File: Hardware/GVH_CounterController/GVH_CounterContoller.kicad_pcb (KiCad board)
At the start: 2 copper layers, 82.5 x 88.9 mm, 74 parts, among them J1 Molex Ultra-Fit, J10 Molex Micro-Fit 2pos, J11 Molex Micro-Fit 2pos, J12 Molex Micro-Fit 2pos, J13 Molex Micro-Fit 3pos, J2 Molex Micro-Fit 2pos, J3 WIZnet_J1B1211CCD_RJ45, J4 Molex Micro-Fit 5pos, J5 Molex Micro-Fit 5pos, J6 Molex Micro-Fit 5pos, J7 Molex Micro-Fit 5pos, J8 Molex Micro-Fit 2pos, J9 Molex Micro-Fit 2pos, K1 Relay_DPDT, Q1 MBT2222, Q2 AO3406, Q3 AO3406, SW1 SW_DIP_x02, SW2 SW_MEC_5G, U1 Teensy4.1, U10 74LVC2G125DC,125, U11 74LVC2G125DC,125, U12 74LVC2G125DC,125, U14 SN74LVC2G17, U2 R-78E5.0-1.0, U3 RT9080-3.3, U4 DS18B20_, U5 74LVC2G125DC,125, U6 74LVC2G125DC,125, U7 74LVC2G125DC,125, U8 74LVC2G125DC,125, U9 74LVC2G125DC,125

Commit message: Checkpoint before rerouting the power supply
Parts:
- moved J13 89.5 mm to (90.4, 102.8)
- moved R7 7.39 mm to (151.4, 64.0), turned to -90 degrees
- moved C3 1.30 mm to (139.7, 114.3)
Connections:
- SW2 pad 2: BUTTON -> GND
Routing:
- net +12V: track 35.6 -> 125.1 mm
- net +3.3V: track 94.7 -> 171.7 mm, vias 2 -> 1
- net +5V: track 78.7 -> 130.2 mm

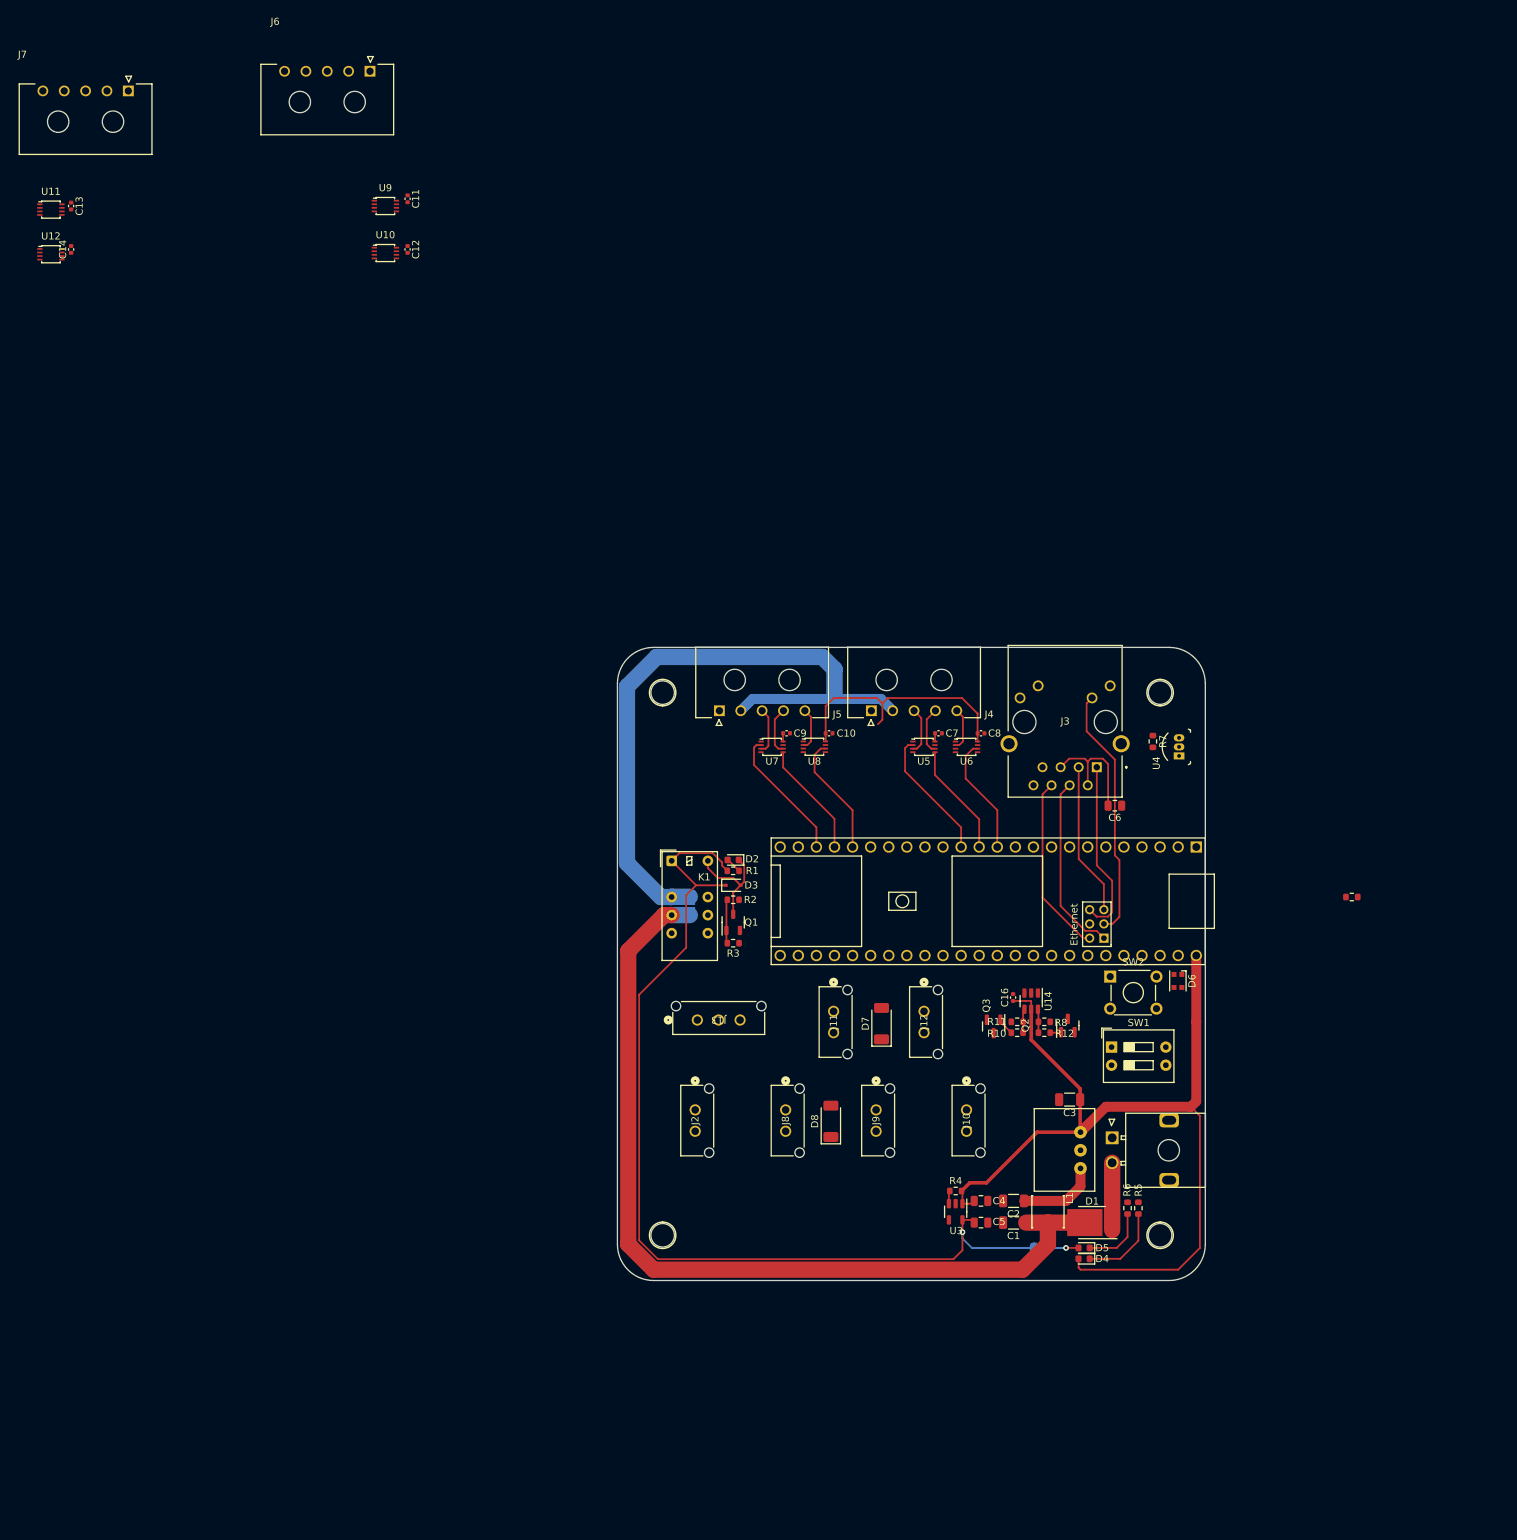
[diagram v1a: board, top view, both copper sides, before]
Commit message: Added header for two board stack design
This will allow the fans to be connected horizontally
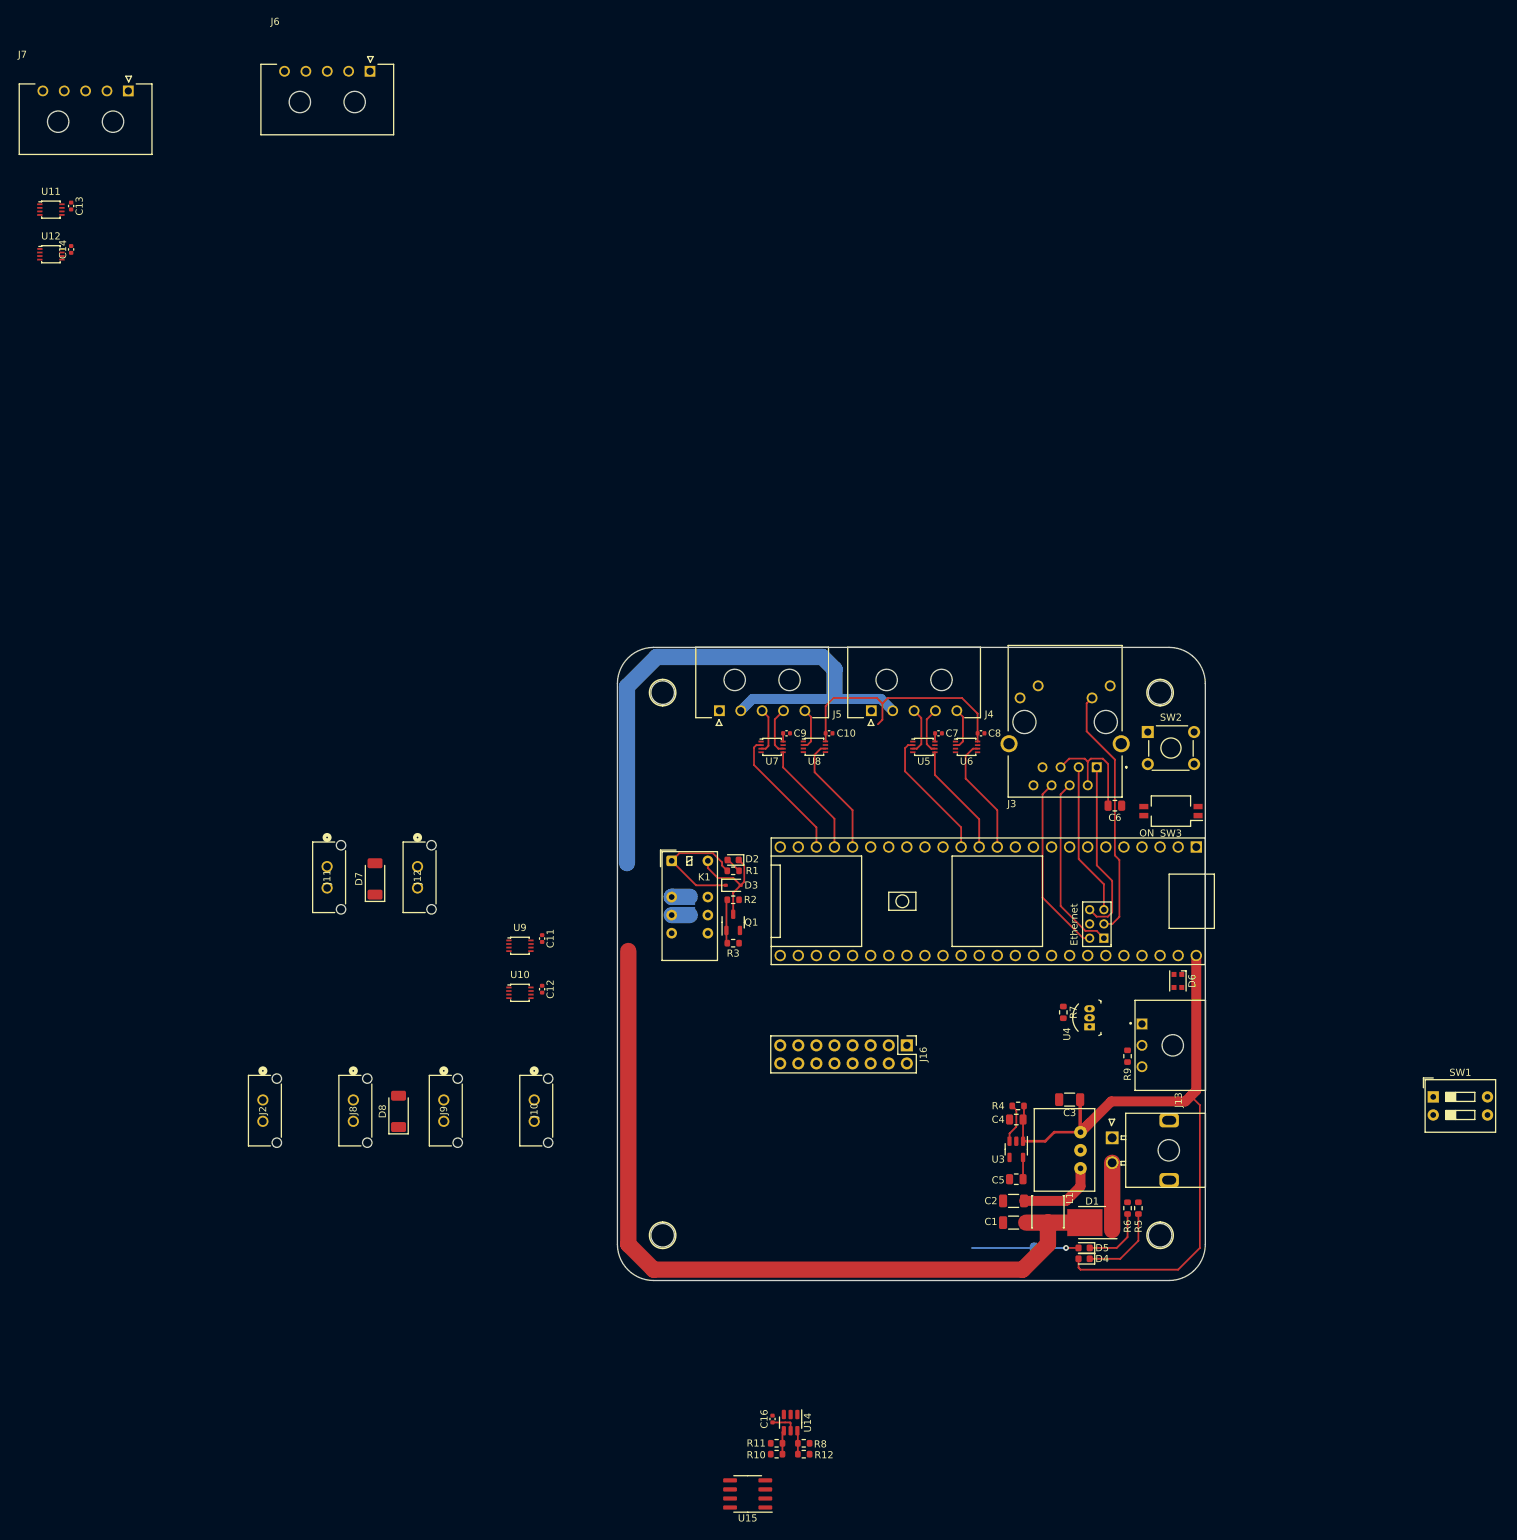
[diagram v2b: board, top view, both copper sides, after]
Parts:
- removed Q2, Q3: AO3406, Package_TO_SOT_SMD:SOT-23
- added J16: Conn_02x08_Odd_Even, Connector_PinHeader_2.54mm:PinHeader_2x08_P2.54mm_Vertical, F.Cu at (116.8, 106.7)
- added SW3: SW_DIP_x02, Button_Switch_SMD:SW_DIP_SPSTx02_Slide_KingTek_DSHP02TS_W7.62mm_P1.27mm, F.Cu at (153.9, 73.8)
- added U15: AO4882, Package_SO:SOIC-8_3.9x4.9mm_P1.27mm, F.Cu at (94.5, 169.7)
- J13: footprint 0_connector:MOLEX_MICROFIT-VERT-3POS_436500315 -> 0_connector:MOLEX_MICROFIT-RA-3POS_436500300
- moved U10 105.6 mm to (62.5, 99.3)
- moved C11 105.6 mm to (65.6, 91.7)
- moved C12 105.6 mm to (65.6, 98.8)
- moved U9 105.6 mm to (62.5, 92.7)
- moved D7 74.0 mm to (42.2, 83.3)
- moved J11 74.0 mm to (35.7, 83.1)
- moved J12 74.0 mm to (48.4, 83.1)
- moved C16 68.1 mm to (98.0, 159.1)
- moved R12 68.1 mm to (102.4, 162.6)
- moved R8 68.1 mm to (102.4, 164.1)
- moved R10 68.1 mm to (98.6, 164.1)
- moved R11 68.1 mm to (98.6, 162.6)
- moved U14 68.1 mm to (100.5, 159.7)
- moved J10 60.7 mm to (64.8, 115.8)
- moved J2 60.7 mm to (26.7, 115.8)
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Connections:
- net Net-(J4-Pin_3) renamed /IO_Level_Shift/CLK_OUT
- net Net-(J4-Pin_4) renamed /IO_Level_Shift/LOAD_OUT
- net Net-(J4-Pin_5) renamed /IO_Level_Shift/SERIAL_IN
- net Net-(J5-Pin_3) renamed /IO_Level_Shift1/CLK_OUT
- net Net-(J5-Pin_4) renamed /IO_Level_Shift1/LOAD_OUT
- net Net-(J5-Pin_5) renamed /IO_Level_Shift1/SERIAL_IN
- U10 pad 2: Net-(J6-Pin_5) -> /IO_Level_Shift2/SERIAL_IN
- U10 pad 6: /IO_Level_Shift2/SERIAL_IN -> (no net)
- U11 pad 2: /IO_Level_Shift3/LOAD -> (no net)
- U11 pad 3: Net-(J7-Pin_3) -> (no net)
- U11 pad 5: /IO_Level_Shift3/CLK -> (no net)
- U11 pad 6: Net-(J7-Pin_4) -> (no net)
- U12 pad 2: Net-(J7-Pin_5) -> /IO_Level_Shift3/SERIAL_IN
- U12 pad 6: /IO_Level_Shift3/SERIAL_IN -> (no net)
- U9 pad 2: /IO_Level_Shift2/LOAD -> (no net)
- U9 pad 3: Net-(J6-Pin_3) -> (no net)
- U9 pad 5: /IO_Level_Shift2/CLK -> (no net)
- U9 pad 6: Net-(J6-Pin_4) -> (no net)
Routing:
- net +3.3V: track 171.7 -> 65.7 mm, vias 1 -> 0
- net +5V: track 130.2 -> 105.1 mm
- net +12V_ISO: track 93.5 -> 85.3 mm
- net +12V: track 125.1 -> 116.9 mm
- net Net-(U3-EN): track 1.83 -> 5.58 mm
- net Net-(R10-Pad2): track 2.45 -> 0.00 mm
- net Net-(R8-Pad2): track 1.55 -> 0.00 mm
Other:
- board text added: "ON"

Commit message: Checkpoint before removing fan connectors
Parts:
- removed J6, J7: Molex Micro-Fit 5pos, 0_connector:MOLEX_MICROFIT-RA-5POS_436500500
- removed JP1: SolderJumper_2_Open, Jumper:SolderJumper-2_P1.3mm_Open_RoundedPad1.0x1.5mm
- removed SW1: SW_DIP_x02, Button_Switch_THT:SW_DIP_SPSTx02_Slide_9.78x7.26mm_W7.62mm_P2.54mm
- JP2: moved to F.Cu
- moved U12 162.8 mm to (118.6, 103.4)
- moved U11 162.8 mm to (112.8, 103.4)
- moved C14 160.9 mm to (120.4, 101.1)
- moved C13 160.8 mm to (114.6, 101.1), turned to 90 degrees
- moved C16 64.0 mm to (126.7, 102.0)
- moved R10 64.0 mm to (127.3, 106.9)
- moved R11 64.0 mm to (127.3, 105.4)
- moved R12 64.0 mm to (131.1, 105.4)
- moved R8 64.0 mm to (131.1, 106.9)
- moved U14 64.0 mm to (129.2, 102.5)
- moved U15 49.5 mm to (115.6, 124.9), turned to -90 degrees
- moved U10 44.6 mm to (106.9, 103.4)
- moved C12 43.1 mm to (108.7, 101.1), turned to 90 degrees
- moved U9 40.0 mm to (101.1, 103.4)
- moved C11 38.4 mm to (102.8, 101.1), turned to 90 degrees
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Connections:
- J16 pad 1: unconnected-(J16-Pin_1-Pad1) -> +5V
- J16 pad 11: unconnected-(J16-Pin_11-Pad11) -> LD_2_OUT
- J16 pad 12: unconnected-(J16-Pin_12-Pad12) -> GND
- J16 pad 13: unconnected-(J16-Pin_13-Pad13) -> CLK_2_OUT
- J16 pad 14: unconnected-(J16-Pin_14-Pad14) -> GND
- J16 pad 15: (no net) -> +12V_ISO
- J16 pad 16: (no net) -> +12V
- J16 pad 2: unconnected-(J16-Pin_2-Pad2) -> +3.3V
- J16 pad 3: unconnected-(J16-Pin_3-Pad3) -> SER_3_OUT
- J16 pad 5: unconnected-(J16-Pin_5-Pad5) -> LD_3_OUT
- J16 pad 7: unconnected-(J16-Pin_7-Pad7) -> CLK_3_OUT
- J16 pad 9: unconnected-(J16-Pin_9-Pad9) -> SER_2_OUT
- R1 pad 1: +3.3V -> Net-(D2-A)
- R1 pad 2: Net-(D2-A) -> +3.3V
- SW3 pad 1: unconnected-(SW3-Pad1) -> GND
- SW3 pad 2: unconnected-(SW3-Pad2) -> GND
- SW3 pad 3: unconnected-(SW3-Pad3) -> DIP_1
- SW3 pad 4: unconnected-(SW3-Pad4) -> DIP_0
- U1 pad 2: unconnected-(U1-0_RX1_CRX2_CS1-Pad2) -> DIP_0
- U1 pad 25: unconnected-(U1-33_MCLK2-Pad25) -> LOAD_2
- U1 pad 26: unconnected-(U1-34_RX8-Pad26) -> CLK_2
- U1 pad 27: unconnected-(U1-35_TX8-Pad27) -> SER_2
- U1 pad 3: unconnected-(U1-1_TX1_CTX2_MISO1-Pad3) -> DIP_1
- U1 pad 35: unconnected-(U1-13_SCK_LED-Pad35) -> LOAD_3
- U1 pad 36: unconnected-(U1-14_A0_TX3_SPDIF_OUT-Pad36) -> CLK_3
- U1 pad 37: unconnected-(U1-15_A1_RX3_SPDIF_IN-Pad37) -> SER_3
- U1 pad 4: unconnected-(U1-2_OUT2-Pad4) -> BUTTON
- U10 pad 2: /IO_Level_Shift2/SERIAL_IN -> SER_2_OUT
- U10 pad 6: (no net) -> SER_2
- U11 pad 2: (no net) -> LOAD_3
- U11 pad 3: (no net) -> CLK_3_OUT
- U11 pad 5: (no net) -> CLK_3
- U11 pad 6: (no net) -> LD_3_OUT
- U12 pad 2: /IO_Level_Shift3/SERIAL_IN -> SER_3_OUT
- U12 pad 6: (no net) -> SER_3
- U9 pad 2: (no net) -> LOAD_2
- U9 pad 3: (no net) -> CLK_2_OUT
- U9 pad 5: (no net) -> CLK_2
- U9 pad 6: (no net) -> LD_2_OUT
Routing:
- net +5V: track 105.1 -> 363.2 mm, vias 0 -> 7
- net +3.3V: track 65.7 -> 290.4 mm, vias 0 -> 2
- net +12V_ISO: track 85.3 -> 131.0 mm
- net +12V: track 116.9 -> 144.0 mm, vias 0 -> 2
- net BUTTON: track 0.00 -> 23.9 mm
- net SER_2: track 0.00 -> 11.7 mm
- net SER_3: track 0.00 -> 11.3 mm
- net CLK_3: track 0.00 -> 11.3 mm
- net CLK_2: track 0.00 -> 11.2 mm
- net LOAD_2: track 0.00 -> 10.5 mm
- net LOAD_3: track 0.00 -> 10.2 mm
- net GND: track 0.00 -> 9.93 mm
- net CLK_3_OUT: track 0.00 -> 9.69 mm
- net LD_3_OUT: track 0.00 -> 9.65 mm
- net SER_3_OUT: track 0.00 -> 9.55 mm
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- added copper zone on B.Cu, net GND
- added copper zone on F.Cu, net GND

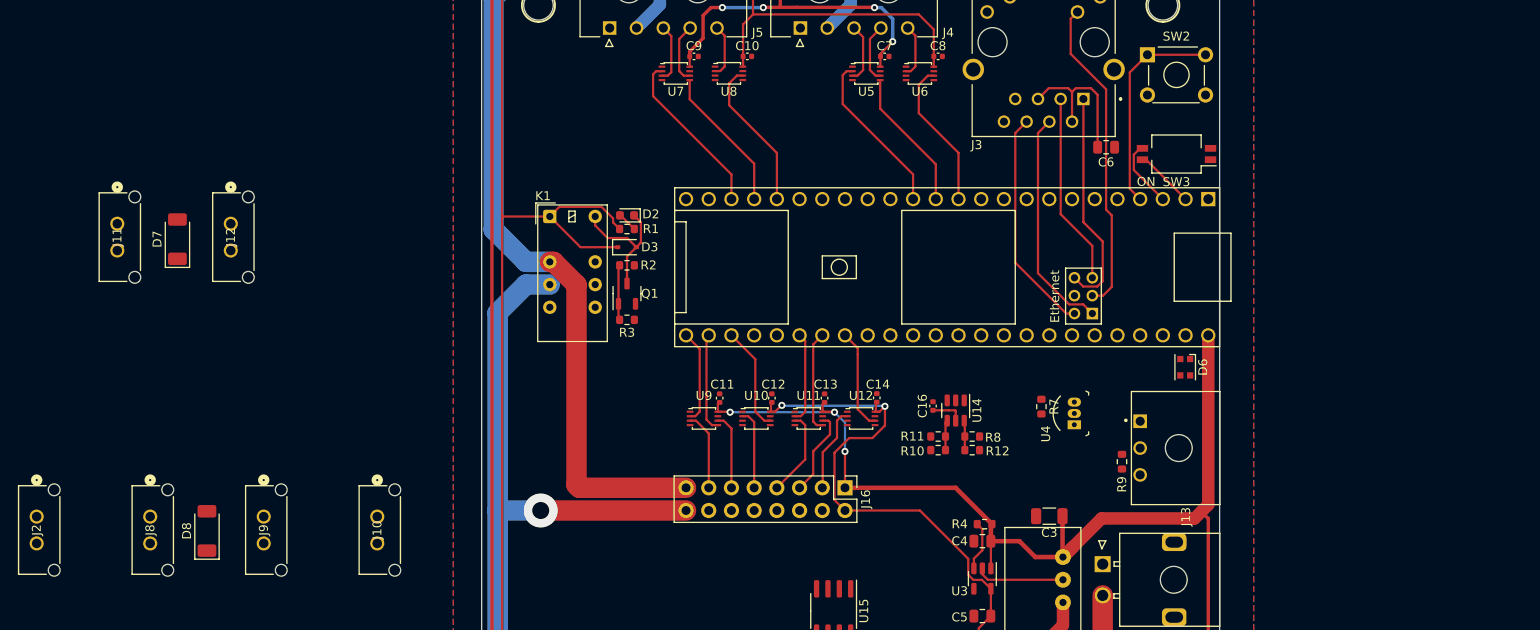
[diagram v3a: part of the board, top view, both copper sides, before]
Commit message: Noticed that voltage translators wont work 3-5v, changing that part
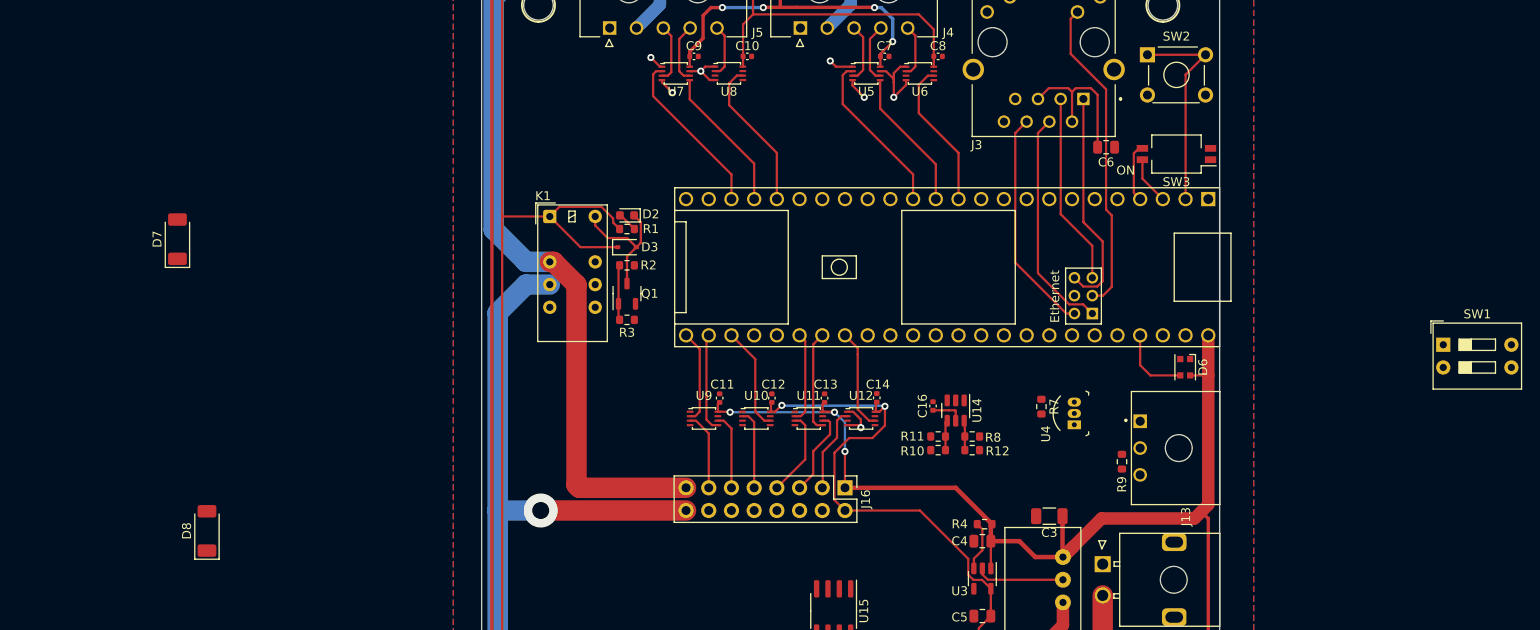
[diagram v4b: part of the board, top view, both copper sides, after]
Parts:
- removed J10, J11, J12, J2, J8, J9: Molex Micro-Fit 2pos, 0_connector:MOLEX_MICROFIT-VERT-2POS_436500215
- added SW1: SW_DIP_x02, Button_Switch_THT:SW_DIP_SPSTx02_Slide_9.78x7.26mm_W7.62mm_P2.54mm, F.Cu at (183.8, 95.1)
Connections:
- R1 pad 1: Net-(D2-A) -> +3.3V
- R1 pad 2: +3.3V -> Net-(D2-A)
- U1 pad 2: DIP_0 -> BUTTON
- U1 pad 3: DIP_1 -> DIP_0
- U1 pad 4: BUTTON -> DIP_1
- U1 pad 45: unconnected-(U1-23_A9_CRX1_MCLK1-Pad45) -> STATUS_PIXEL
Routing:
- net GND: track 9.93 -> 37.3 mm, vias 0 -> 7
- net STATUS_PIXEL: track 0.00 -> 8.30 mm
- net +5V: track 363.2 -> 365.3 mm
- net DIP_0: track 6.65 -> 5.35 mm
- net DIP_1: track 7.57 -> 6.60 mm
